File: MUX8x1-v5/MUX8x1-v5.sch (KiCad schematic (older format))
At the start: 49 parts, among them J1 Conn_01x09_Male, J10 Conn_01x03_Male, J11 Conn_01x09_Male, J12 Conn_01x09_Male, J14 Conn_01x09_Male, J15 Conn_01x09_Male, J16 Conn_01x09_Male, J18 Conn_01x09_Male, J2 Conn_01x09_Male, J20 Conn_01x01_Male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

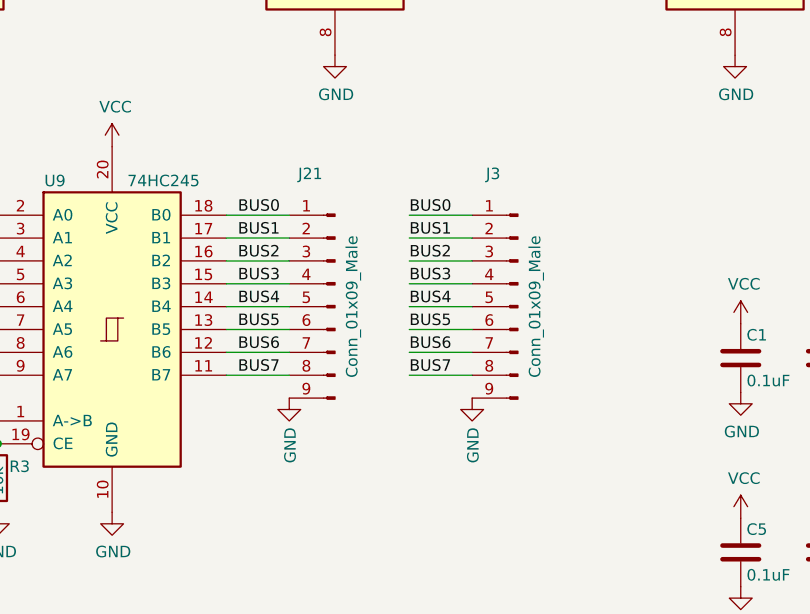
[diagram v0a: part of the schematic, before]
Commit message: Polishing MUX8:1
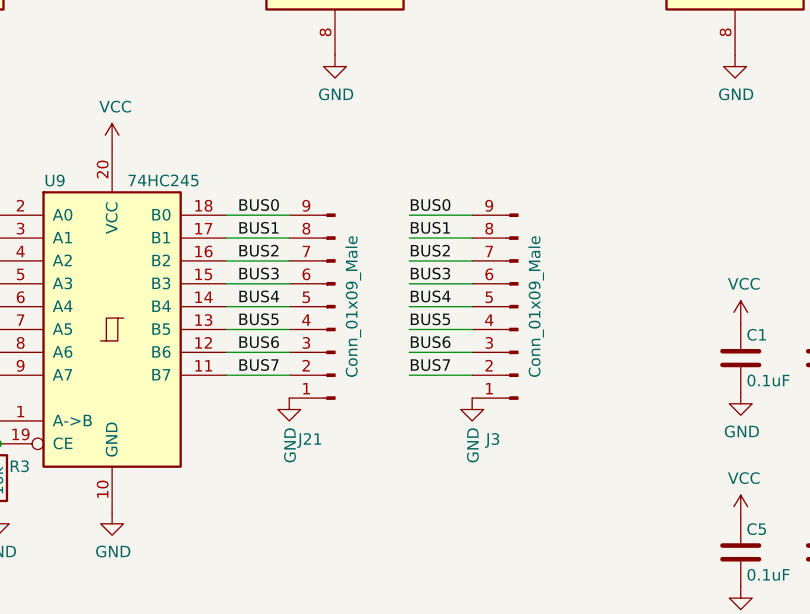
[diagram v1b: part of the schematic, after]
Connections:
- net BUS0: now also J21.9 (Pin_9), J3.9 (Pin_9); no longer J21.1 (Pin_1), J3.1 (Pin_1)
- net BUS1: now also J21.8 (Pin_8), J3.8 (Pin_8); no longer J21.2 (Pin_2), J3.2 (Pin_2)
- net BUS2: now also J21.7 (Pin_7), J3.7 (Pin_7); no longer J21.3 (Pin_3), J3.3 (Pin_3)
- net BUS3: now also J21.6 (Pin_6), J3.6 (Pin_6); no longer J21.4 (Pin_4), J3.4 (Pin_4)
- net BUS5: now also J21.4 (Pin_4), J3.4 (Pin_4); no longer J21.6 (Pin_6), J3.6 (Pin_6)
- net BUS6: now also J21.3 (Pin_3), J3.3 (Pin_3); no longer J21.7 (Pin_7), J3.7 (Pin_7)
- net BUS7: now also J21.2 (Pin_2), J3.2 (Pin_2); no longer J21.8 (Pin_8), J3.8 (Pin_8)
- net GND: now also J21.1 (Pin_1), J3.1 (Pin_1); no longer J21.9 (Pin_9), J3.9 (Pin_9)
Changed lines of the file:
@@
 F 3 "~" H 3125 6275 50  0001 C CNN
 	1    3125 6275
-	-1   0    0    -1
+	-1   0    0    1
 $EndComp
 $Comp
@@
 F 3 "~" H 3925 6275 50  0001 C CNN
 	1    3925 6275
-	-1   0    0    -1
-$EndComp
-$Comp
+	-1   0    0    1
+$EndComp
+$Comp

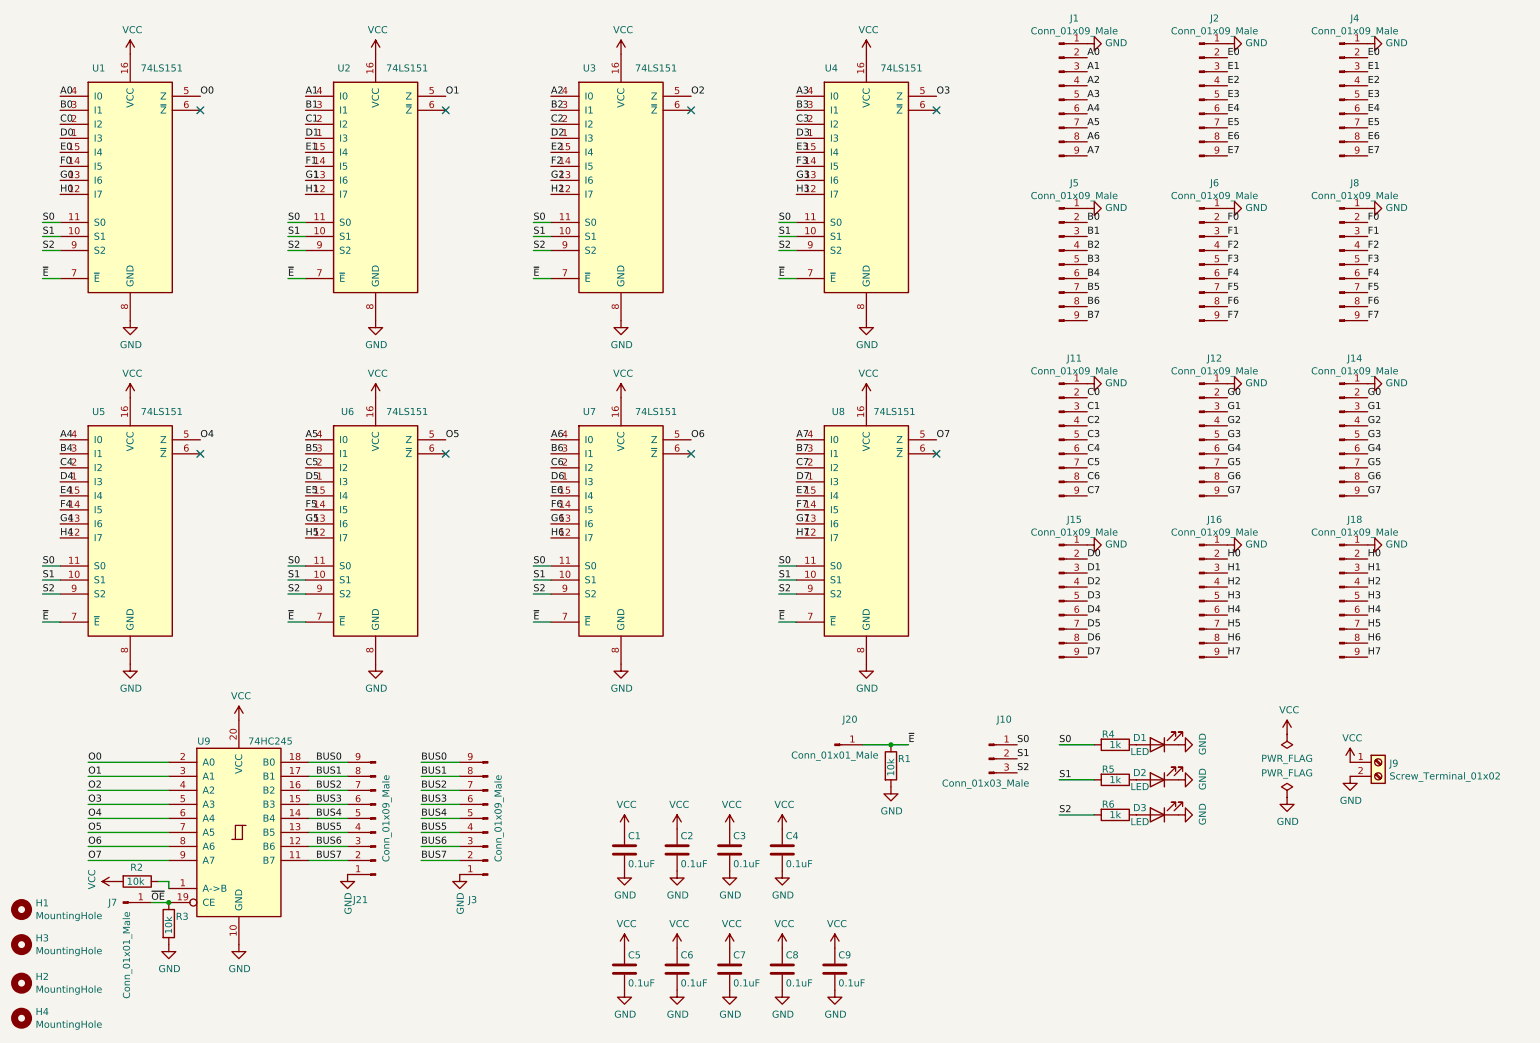
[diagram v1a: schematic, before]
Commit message: MUX8:1 - Now it have 2 zero line
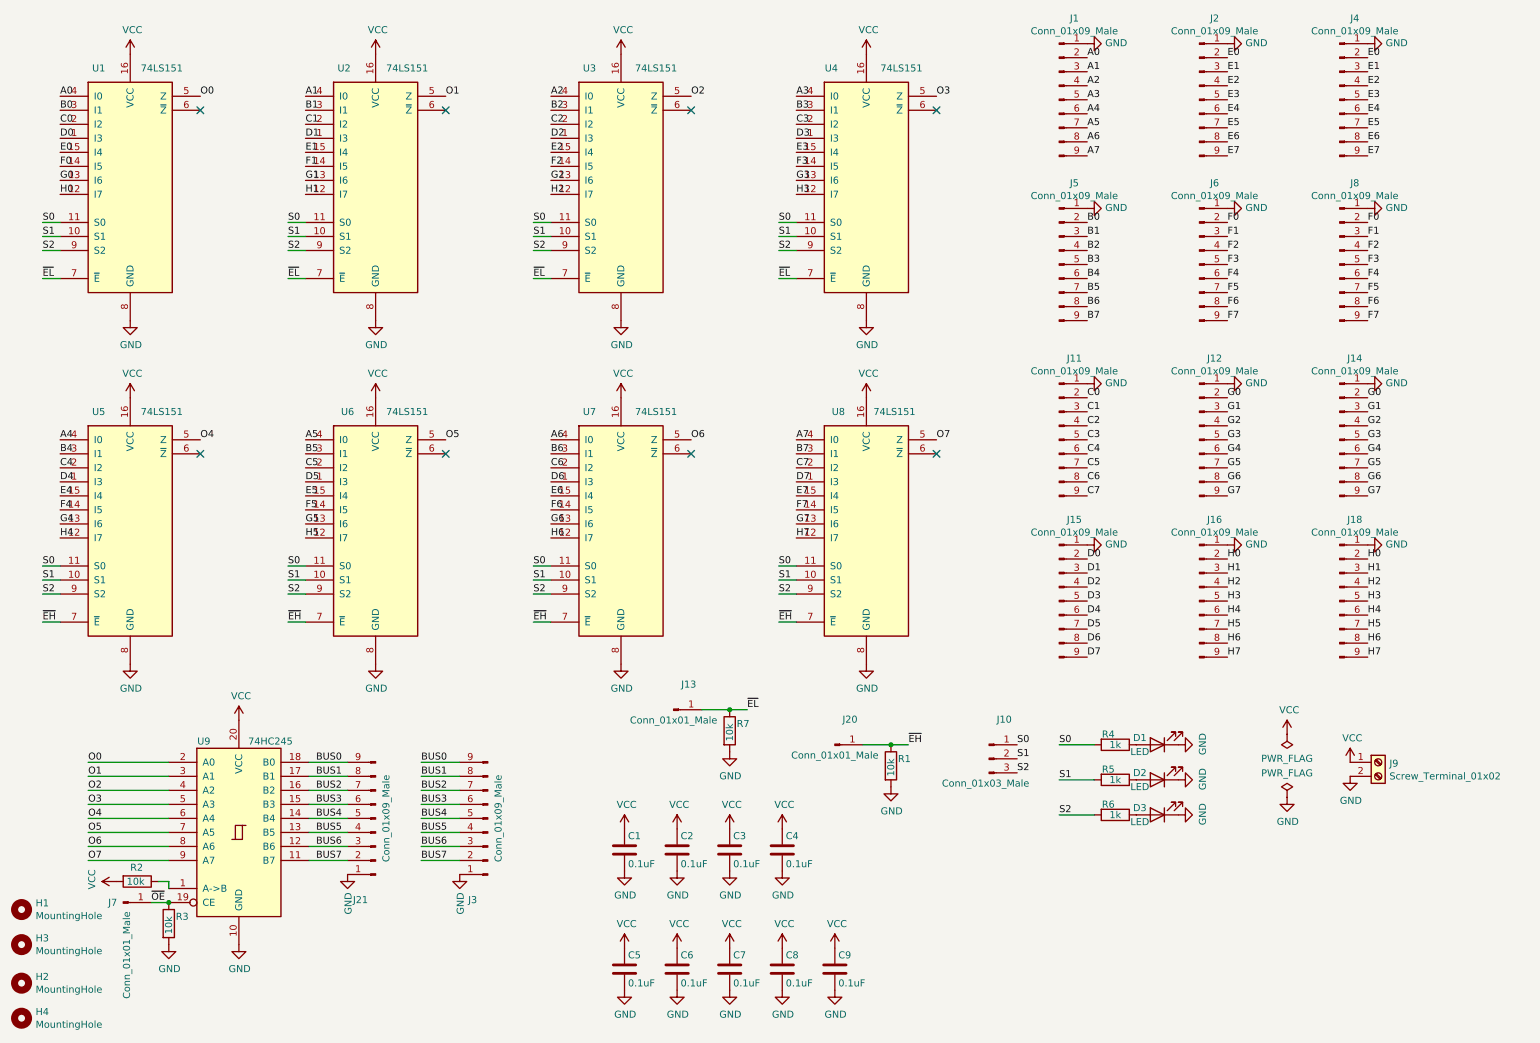
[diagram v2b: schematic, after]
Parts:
- added J13: Conn_01x01_Male, Connector_PinHeader_2.54mm:PinHeader_1x01_P2.54mm_Vertical, symbol Connector:Conn_01x01_Male
- added R7: 10k, Resistor_SMD:R_0805_2012Metric_Pad1.20x1.40mm_HandSolder, symbol Device:R
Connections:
- net GND: now also R7.2
- net ~E renamed ~EH
- net ~EH: no longer U1.7 (~E), U2.7 (~E), U3.7 (~E), U4.7 (~E)
- new net ~EL: J13.1 (Pin_1), R7.1, U1.7 (~E), U2.7 (~E), U3.7 (~E), U4.7 (~E)
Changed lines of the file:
@@
 H7
 Text Label 750  2425 0    50   ~ 0
-~E
+~EL
 Wire Wire Line
 	750  2425 875  2425
 Text Label 2500 2425 0    50   ~ 0
-~E
+~EL
 Wire Wire Line
 	2500 2425 2625 2425
 Text Label 4250 2425 0    50   ~ 0
-~E
+~EL
 Wire Wire Line
 	4250 2425 4375 2425
 Text Label 6000 2425 0    50   ~ 0
-~E
+~EL
 Wire Wire Line
 	6000 2425 6125 2425
 Text Label 750  4875 0    50   ~ 0
-~E
+~EH
 Wire Wire Line
 	750  4875 875  4875
 Text Label 2500 4875 0    50   ~ 0
-~E
+~EH
 Wire Wire Line
 	2500 4875 2625 4875
 Text Label 4250 4875 0    50   ~ 0
-~E
+~EH
 Wire Wire Line
 	4250 4875 4375 4875
 Text Label 6000 4875 0    50   ~ 0
-~E
+~EH
 Wire Wire Line
 	6000 4875 6125 4875
@@
 $EndComp
 Text Label 6925 5750 0    50   ~ 0
-~E
+~EH
 Wire Wire Line
 	6925 5750 6800 5750
@@
 Text Label 8000 6250 0    50   ~ 0
 S2
+$Comp
+L Connector:Conn_01x01_Male J13
+U 1 1 64C4AD0D
+P 5250 5500
+F 0 "J13" H 5358 5681 50  0000 C CNN
+F 1 "Conn_01x01_Male" H 5250 5425 50  0000 C CNN
+F 2 "Connector_PinHeader_2.54mm:PinHeader_1x01_P2.54mm_Vertical" H 5250 5500 50  0001 C CNN
+F 3 "~" H 5250 5500 50  0001 C CNN
+	1    5250 5500
+	1    0    0    -1
+$EndComp
+Text Label 5775 5500 0    50   ~ 0
+~EL
+Wire Wire Line
+	5775 5500 5650 5500
+$Comp
+L Device:R R7
+U 1 1 64C4AD15
+P 5650 5650
+F 0 "R7" H 5700 5700 50  0000 L CNN
+F 1 "10k" V 5650 5575 50  0000 L CNN
+F 2 "Resistor_SMD:R_0805_2012Metric_Pad1.20x1.40mm_HandSolder" V 5580 5650 50  0001 C CNN
+F 3 "~" H 5650 5650 50  0001 C CNN
+	1    5650 5650
+	1    0    0    -1
+$EndComp
+Connection ~ 5650 5500
+Wire Wire Line
+	5650 5500 5450 5500
+$Comp
+L power:GND #PWR0104
+U 1 1 64C4AD1D
+P 5650 5800
+F 0 "#PWR0104" H 5650 5550 50  0001 C CNN
+F 1 "GND" H 5655 5627 50  0000 C CNN
+F 2 "" H 5650 5800 50  0001 C CNN
+F 3 "" H 5650 5800 50  0001 C CNN
+	1    5650 5800
+	1    0    0    -1
+$EndComp
 $EndSCHEMATC
